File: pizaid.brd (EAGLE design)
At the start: 85 x 56 mm, 44 parts, among them X1 S4B-ZR, X2 DCJACK-R

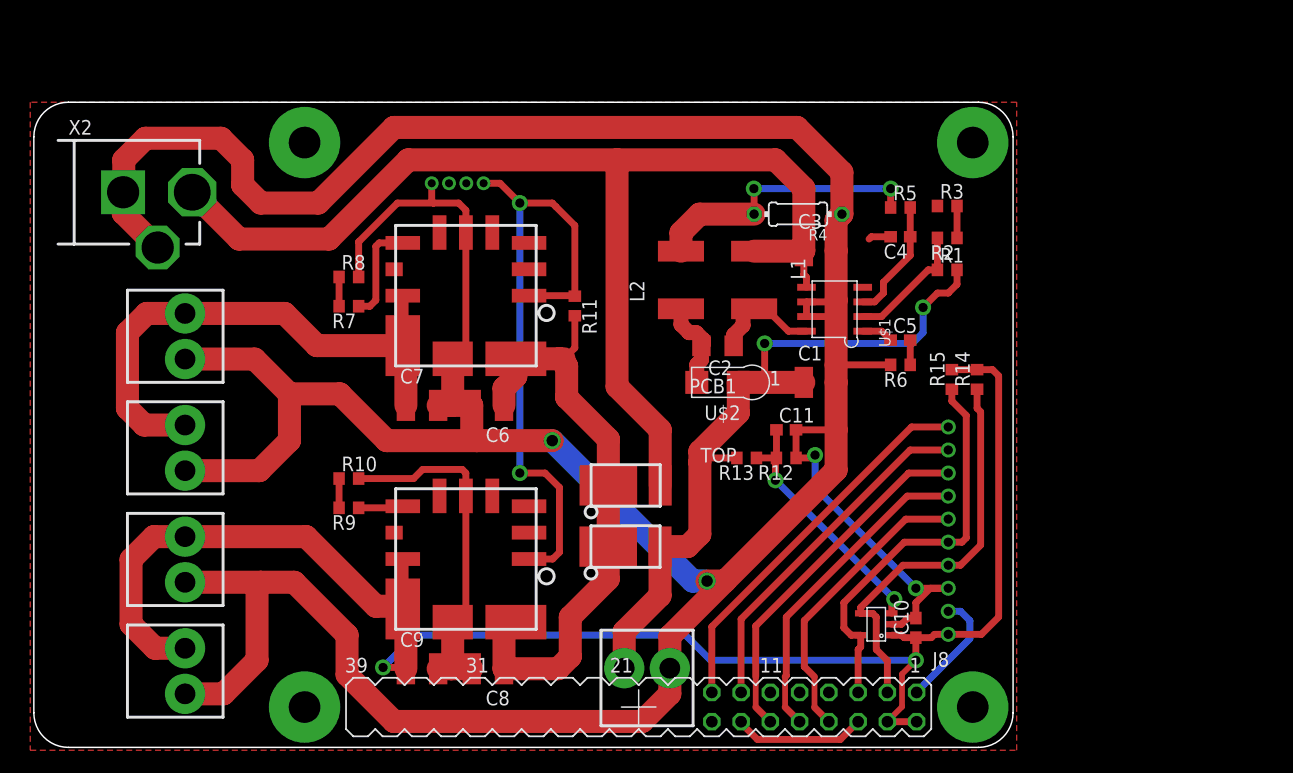
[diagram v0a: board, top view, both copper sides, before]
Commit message: modified board for stacking (ontheway)
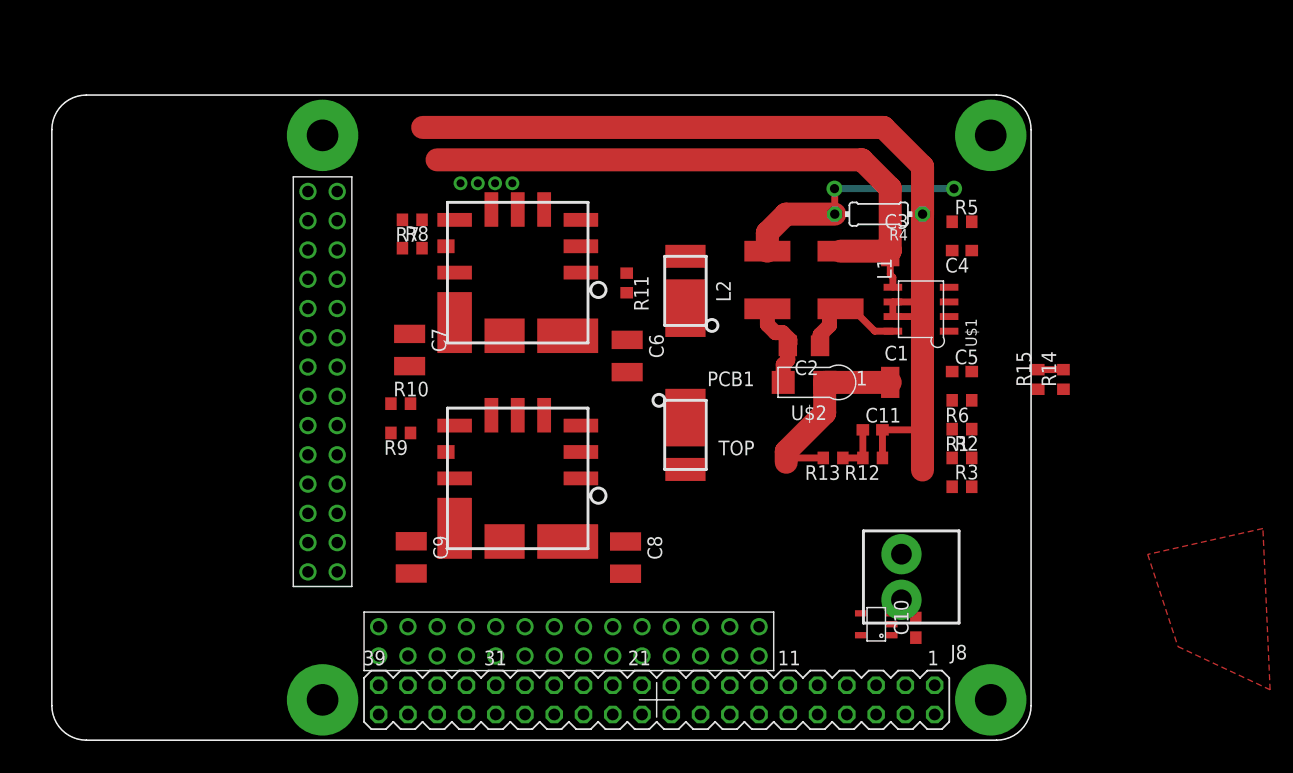
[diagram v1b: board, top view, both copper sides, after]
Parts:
- removed S1: 10B-PH, con-jst:S10B-PH
- removed U$14, U$15, U$9: B2P-VH, pizaid:B2P-VH
- removed X2: DCJACK-R, kamiki-dcjack:2DC-0005D100-R
- added U$3: CON_14X2, pizaid:CON_14X2
- PCB1: device pizaid:RASPBERRY_PI_B+ -> RASPBERRY_PI_Bplus:RASPBERRY_PI_B+
- U$8: value B2P-VH -> CON_14X2; device pizaid:B2P-VH -> pizaid:CON_14X2
- moved U$8 52.2 mm to (66.4, 13.8), turned to 180 degrees
- moved R3 24.4 mm to (84.0, 26.0)
- moved U$10 23.5 mm to (78.8, 18.2), turned to 90 degrees
- moved R2 19.1 mm to (84.0, 28.5), turned to 0 degrees
- moved U$5 17.7 mm to (60.0, 43.0), turned to 270 degrees
- moved C8 15.4 mm to (54.8, 19.8), turned to 270 degrees
- moved R1 13.9 mm to (84.0, 31.0), turned to 180 degrees
- moved C6 12.8 mm to (54.9, 37.3), turned to 270 degrees
- moved U$4 11.0 mm to (60.0, 30.5), turned to 90 degrees
- moved C9 9.71 mm to (36.2, 19.9), turned to 270 degrees
- moved R7 9.30 mm to (36.3, 49.2)
- moved U$7 8.32 mm to (45.4, 26.7)
- moved R10 7.91 mm to (35.3, 33.2)
- moved R9 7.91 mm to (35.3, 30.7)
- moved C1 7.50 mm to (79.2, 35.1)
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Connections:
- removed net 3V3@1: PCB1.1, S1.P$2
- removed net GND@1: PCB1.9
- removed net N$23: PCB1.13, S1.P$9
- new net B$1: PCB1.13, U$8.P$2
- new net B1: PCB1.15, U$8.P$4
- new net B10: PCB1.33, U$8.P$22
- new net B11: PCB1.35, U$8.P$24
- new net B12: PCB1.37, U$8.P$26
- new net B13: U$8.P$28
- new net B2: C10.1, PCB1.1, R14.2, R15.2, U$16.P$1, U$8.P$6
- new net B3: U$8.P$8
- new net B4: PCB1.21, U$8.P$10
- new net B5: PCB1.23, U$8.P$12
- new net B6: U$8.P$14
- new net B7: U$8.P$16
- new net B8: PCB1.29, U$8.P$18
- new net B9: PCB1.31, U$8.P$20
- new net GND@3: PCB1.25, PCB1.39, PCB1.9
- new net N$24: PCB1.26, U$8.P$13
- new net N$25: PCB1.24, U$8.P$11
- new net N$26: PCB1.22, U$8.P$9
- new net N$27: PCB1.18, U$8.P$5
- new net N$28: PCB1.16, U$8.P$3
- net 5V0@2: now also U$3.P$19, U$3.P$20, U$3.P$21, U$3.P$22, U$3.P$23; no longer C10.1, R14.2, R15.2, S1.P$1, U$14.P$1, U$16.P$1, U$9.P$1
- net GND: now also U$3.P$14, U$3.P$15, U$3.P$16, U$3.P$17, U$3.P$18, U$3.P$24, U$3.P$25, U$3.P$26, U$3.P$27, U$3.P$28, U$3.P$5, U$3.P$6, U$3.P$7, U$3.P$8; no longer S1.P$3, U$14.P$2, U$15.P$2, U$8.P$2, U$9.P$2, X2.2, X2.3
- net GND@4: now also PCB1.20, PCB1.30, PCB1.34, U$8.P$1, U$8.P$17, U$8.P$21, U$8.P$7
- net JNET: now also U$3.P$10, U$3.P$11, U$3.P$12, U$3.P$13, U$3.P$9; no longer U$15.P$1, U$8.P$1
- net N$13: now also PCB1.38, U$8.P$25; no longer PCB1.8, S1.P$6
- net N$16: no longer S1.P$5
- net N$20: no longer S1.P$4
- net N$21: now also PCB1.36, U$8.P$23; no longer PCB1.10, S1.P$7
- net N$22: now also PCB1.32, U$8.P$19; no longer PCB1.12, S1.P$8
- net N$9: now also PCB1.40, U$8.P$27; no longer PCB1.15, S1.P$10
- net VCC: now also U$3.P$1, U$3.P$2, U$3.P$3, U$3.P$4; no longer X2.1
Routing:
- net GND: track 380.9 -> 84.8 mm, vias 4 -> 0
- net 5V0@2: track 144.4 -> 0.71 mm, vias 2 -> 0
- net N$12: track 55.5 -> 0.00 mm, vias 2 -> 0
- net N$8: track 52.4 -> 0.00 mm
- net VCC: track 101.5 -> 53.4 mm
- net JNET: track 47.6 -> 0.38 mm
- net N$3: track 64.1 -> 17.4 mm, vias 2 -> 0
- net N$16: track 35.3 -> 0.00 mm
- net N$20: track 35.2 -> 0.00 mm
- net N$9: track 33.4 -> 0.00 mm
- net N$22: track 31.0 -> 0.00 mm
- net N$23: track 30.4 -> 0.00 mm
- net N$21: track 28.1 -> 0.00 mm
- net N$13: track 25.8 -> 0.00 mm
- net N$19: track 22.1 -> 4.18 mm, vias 2 -> 0
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
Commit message: added top board (ontheway)
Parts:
- moved R14 28.7 mm to (73.3, 14.3)
- moved R15 28.7 mm to (71.1, 14.3)
- moved U$10 2.92 mm to (77.2, 20.7)
- moved U$7 0.50 mm to (45.4, 27.2)
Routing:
- net B2: track 2.19 -> 0.00 mm
- net 5V0@2: track 0.71 -> 0.00 mm
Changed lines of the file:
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@@
 <plain>
 <rectangle x1="62.8125" y1="38.75" x2="77.8125" y2="48.75" layer="41"/>
-<rectangle x1="41.8125" y1="23.0625" x2="53.0625" y2="34.3125" layer="41"/>
+<rectangle x1="39.8125" y1="21.5625" x2="51.0625" y2="32.8125" layer="41"/>
 <wire x1="34.5" y1="45.4375" x2="3.125" y2="43.4375" width="0.1" layer="41"/>
 <wire x1="3.4375" y1="24.6875" x2="25.3125" y2="24.6875" width="0.1" layer="41"/>
@@
 <wire x1="34.5" y1="45.4375" x2="34.5" y2="48.875" width="0.1" layer="41"/>
 <rectangle x1="39.8125" y1="38.875" x2="51.0625" y2="50.125" layer="41"/>
-<rectangle x1="93.5625" y1="23" x2="104.8125" y2="34.25" layer="41"/>
 </plain>
 <attributes>
@@
 <element name="U$5" library="pizaid" package="POWERDI5" value="SBR15U50" x="60" y="43" rot="R270"/>
 <element name="U$6" library="pizaid" package="OKL-T/6" value="OKL-T/6" x="45.4425" y="44.585" rot="R180"/>
-<element name="U$7" library="pizaid" package="OKL-T/6" value="OKL-T/6" x="45.4425" y="26.725" rot="R180"/>
+<element name="U$7" library="pizaid" package="OKL-T/6" value="OKL-T/6" x="45.4425" y="27.225" rot="R180"/>
 <element name="C6" library="rcl" package="C3225" value="22u25V" x="54.94" y="37.3475" rot="R270"/>
 <element name="C7" library="rcl" package="C3225" value="22u16V" x="36.06" y="37.8675" rot="R270"/>
@@
 </element>
 <element name="R11" library="rcl" package="R0603" value="10k" x="54.8975" y="43.69" rot="R270"/>
-<element name="U$10" library="pizaid" package="B2P-VH" value="B2P-VH" x="78.75" y="18.165" rot="R90"/>
+<element name="U$10" library="pizaid" package="B2P-VH" value="B2P-VH" x="77.25" y="20.665" rot="R90"/>
 <element name="U$16" library="pizaid" package="SOT-23" value="MCP3021" x="76.5625" y="14.0625" rot="R90"/>
 <element name="C10" library="rcl" package="C0603" value="0.1u" x="80" y="13.75" rot="R90"/>
@@
 <element name="R12" library="rcl" package="R0603" value="10k" x="76.25" y="28.5" rot="R180"/>
 <element name="R13" library="rcl" package="R0603" value="10k" x="72.8125" y="28.5" rot="R180"/>
-<element name="R14" library="rcl" package="R0603" value="2.2k" x="92.8125" y="35.3125" rot="R90"/>
-<element name="R15" library="rcl" package="R0603" value="2.2k" x="90.625" y="35.3125" rot="R90"/>
+<element name="R14" library="rcl" package="R0603" value="2.2k" x="73.3125" y="14.3125" rot="R90"/>
+<element name="R15" library="rcl" package="R0603" value="2.2k" x="71.125" y="14.3125" rot="R90"/>
 <element name="PCB1" library="RASPBERRY_PI_Bplus" package="RASPBERRY_PI_B+" value="RASPBERRY_PI_B+" x="90" y="60" rot="R180"/>
 <element name="U$3" library="pizaid" package="CON_14X2" value="CON_14X2" x="27.23" y="51.63" rot="R270"/>
@@
 <wire x1="45.4425" y1="50.065" x2="40.475" y2="52.3425" width="0" layer="19" extent="1-1"/>
 <wire x1="37.1325" y1="46.7075" x2="40.475" y2="52.3425" width="0" layer="19" extent="1-1"/>
-<wire x1="78.75" y1="20.145" x2="83.15" y2="26" width="0" layer="19" extent="1-1"/>
-<wire x1="80" y1="14.6" x2="78.75" y2="20.145" width="0" layer="19" extent="1-1"/>
+<wire x1="77.25" y1="22.645" x2="83.15" y2="26" width="0" layer="19" extent="1-1"/>
+<wire x1="80" y1="14.6" x2="77.25" y2="22.645" width="0" layer="19" extent="1-1"/>
 <wire x1="77.9125" y1="14.0625" x2="80" y2="14.6" width="0" layer="19" extent="1-1"/>
 <wire x1="29.77" y1="46.55" x2="37.1325" y2="46.7075" width="0" layer="19" extent="1-1"/>
@@
 <wire x1="27.23" y1="18.61" x2="29.77" y2="18.61" width="0" layer="19" extent="1-1"/>
 <wire x1="36.2" y1="18.4675" x2="29.77" y2="18.61" width="0" layer="19" extent="1-1"/>
-<wire x1="44.2975" y1="21.245" x2="36.2" y2="18.4675" width="0" layer="19" extent="1-1"/>
+<wire x1="44.2975" y1="21.745" x2="36.2" y2="18.4675" width="0" layer="19" extent="1-1"/>
 <wire x1="44.2975" y1="39.105" x2="36.06" y2="36.4675" width="0" layer="19" extent="1-1"/>
-<wire x1="45.4425" y1="32.205" x2="45.4375" y2="39.1875" width="0" layer="19" extent="1-1"/>
+<wire x1="45.4425" y1="32.705" x2="45.4375" y2="39.1875" width="0" layer="19" extent="1-1"/>
 <wire x1="28.5" y1="56.5" x2="37.1875" y2="57.1875" width="0" layer="19" extent="1-1"/>
 <wire x1="86.5" y1="7.5" x2="80" y2="14.6" width="0" layer="19" extent="1-1"/>
 <wire x1="54.94" y1="35.9475" x2="45.4375" y2="39.1875" width="0" layer="19" extent="1-1"/>
-<wire x1="54.8" y1="18.4475" x2="44.2975" y2="21.245" width="0" layer="19" extent="1-1"/>
+<wire x1="54.8" y1="18.4475" x2="44.2975" y2="21.745" width="0" layer="19" extent="1-1"/>
 <wire x1="28.5" y1="7.5" x2="29.77" y2="18.61" width="0" layer="19" extent="1-1"/>
 </signal>
@@
 <wire x1="77.775" y1="35.0575" x2="83.15" y2="31" width="0" layer="19" extent="1-1"/>
 <wire x1="60" y1="27.5" x2="68.75" y2="28.125" width="0" layer="19" extent="1-1"/>
-<wire x1="78.75" y1="16.185" x2="71.9625" y2="28.5" width="0" layer="19" extent="1-1"/>
+<wire x1="77.25" y1="18.685" x2="71.9625" y2="28.5" width="0" layer="19" extent="1-1"/>
 <wire x1="77.775" y1="35.0575" x2="72.085" y2="35.0575" width="2" layer="1"/>
 </signal>
@@
 <wire x1="54.8" y1="21.2475" x2="60.795" y2="26.1" width="0" layer="19" extent="1-1"/>
 <wire x1="60" y1="32" x2="54.8" y2="21.2475" width="0" layer="19" extent="1-1"/>
-<wire x1="49.7775" y1="21.245" x2="54.8" y2="21.2475" width="0" layer="19" extent="1-1"/>
+<wire x1="49.7775" y1="21.745" x2="54.8" y2="21.2475" width="0" layer="19" extent="1-1"/>
 </signal>
 <signal name="N$14">
 <contactref element="U$7" pad="P$6"/>
 <contactref element="R9" pad="1"/>
-<wire x1="39.8275" y1="31.17" x2="39.9625" y2="31.305" width="0.6" layer="1"/>
-<wire x1="36.1325" y1="30.67" x2="39.8275" y2="31.17" width="0" layer="19" extent="1-1"/>
+<wire x1="36.1325" y1="30.67" x2="39.9625" y2="31.805" width="0" layer="19" extent="1-1"/>
 </signal>
 <signal name="N$15">
@@
 <wire x1="50.9225" y1="44.585" x2="54.8975" y2="44.54" width="0" layer="19" extent="1-1"/>
 <wire x1="44.975" y1="52.3425" x2="50.9225" y2="44.585" width="0" layer="19" extent="1-1"/>
-<wire x1="50.9225" y1="26.725" x2="50.9225" y2="44.585" width="0" layer="19" extent="1-1"/>
+<wire x1="50.9225" y1="27.225" x2="50.9225" y2="44.585" width="0" layer="19" extent="1-1"/>
 </signal>
 <signal name="N$16">
@@
 <contactref element="R15" pad="1"/>
 <contactref element="PCB1" pad="5"/>
-<wire x1="75.2125" y1="13.1125" x2="90.625" y2="34.4625" width="0" layer="19" extent="1-1"/>
+<wire x1="75.2125" y1="13.1125" x2="71.125" y2="13.4625" width="0" layer="19" extent="1-1"/>
 <wire x1="76.55" y1="8.77" x2="75.2125" y2="13.1125" width="0" layer="19" extent="1-1"/>
 </signal>
@@
 <contactref element="R14" pad="1"/>
 <contactref element="PCB1" pad="3"/>
-<wire x1="75.2125" y1="15.0125" x2="92.8125" y2="34.4625" width="0" layer="19" extent="1-1"/>
+<wire x1="75.2125" y1="15.0125" x2="73.3125" y2="13.4625" width="0" layer="19" extent="1-1"/>
 <wire x1="79.09" y1="8.77" x2="75.2125" y2="15.0125" width="0" layer="19" extent="1-1"/>
 </signal>
@@
 <contactref element="PCB1" pad="2"/>
 <contactref element="PCB1" pad="4"/>
-<wire x1="39.7275" y1="22.625" x2="39.9625" y2="22.39" width="2" layer="1"/>
-<wire x1="40.2325" y1="22.12" x2="39.9625" y2="22.39" width="2" layer="1"/>
 <contactref element="U$3" pad="P$19"/>
 <contactref element="U$3" pad="P$21"/>
@@
 <contactref element="U$3" pad="P$22"/>
 <wire x1="79.09" y1="6.23" x2="81.63" y2="6.23" width="0" layer="19" extent="1-1"/>
-<wire x1="40.2325" y1="22.12" x2="79.09" y2="6.23" width="0" layer="19" extent="1-1"/>
-<wire x1="36.2" y1="21.2675" x2="39.7275" y2="22.625" width="0" layer="19" extent="1-1"/>
-<wire x1="39.9625" y1="26.725" x2="39.7275" y2="22.625" width="0" layer="19" extent="1-1"/>
+<wire x1="39.9625" y1="22.89" x2="79.09" y2="6.23" width="0" layer="19" extent="1-1"/>
+<wire x1="39.9625" y1="27.225" x2="39.9625" y2="22.89" width="0" layer="19" extent="1-1"/>
+<wire x1="36.2" y1="21.2675" x2="39.9625" y2="22.89" width="0" layer="19" extent="1-1"/>
 <wire x1="29.77" y1="26.23" x2="36.2" y2="21.2675" width="0" layer="19" extent="1-1"/>
 <wire x1="29.77" y1="28.77" x2="29.77" y2="26.23" width="0" layer="19" extent="1-1"/>
@@
 <contactref element="R15" pad="2"/>
 <contactref element="R14" pad="2"/>
-<wire x1="90.625" y1="36.1625" x2="92.8125" y2="36.1625" width="0.6" layer="1"/>
-<wire x1="80" y1="12.9" x2="90.625" y2="36.1625" width="0" layer="19" extent="1-1"/>
+<wire x1="71.125" y1="15.1625" x2="73.3125" y2="15.1625" width="0" layer="19" extent="1-16"/>
+<wire x1="80" y1="12.9" x2="71.125" y2="15.1625" width="0" layer="19" extent="1-1"/>
 <wire x1="77.9125" y1="13.1125" x2="80" y2="12.9" width="0" layer="19" extent="1-1"/>
 <wire x1="81.63" y1="8.77" x2="80" y2="12.9" width="0" layer="19" extent="1-1"/>

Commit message: continuing placement.....................
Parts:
- moved U$5 11.8 mm to (62.5, 31.5), turned to 180 degrees
- moved C11 9.51 mm to (76.8, 21.4)
- moved R12 9.51 mm to (76.8, 19.0)
- moved R13 9.51 mm to (73.3, 19.0)
- moved R1 8.00 mm to (84.0, 23.0)
- moved R2 8.00 mm to (84.0, 20.5)
- moved U$10 7.52 mm to (76.8, 28.2)
- moved R3 7.50 mm to (84.0, 18.5)
- moved U$4 4.30 mm to (62.5, 27.0), turned to 180 degrees
- moved R8 2.91 mm to (36.3, 43.8), turned to 270 degrees
- moved R7 1.87 mm to (36.3, 47.3), turned to 270 degrees
- moved C5 1.00 mm to (84.0, 37.0)
- moved R6 1.00 mm to (84.0, 34.5)
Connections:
- net GND: now also U$3.P$1, U$3.P$2, U$3.P$3, U$3.P$4; no longer U$3.P$5, U$3.P$6, U$3.P$7, U$3.P$8
- net VCC: now also U$3.P$5, U$3.P$6, U$3.P$7, U$3.P$8; no longer U$3.P$1, U$3.P$2, U$3.P$3, U$3.P$4
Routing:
- net GND: track 84.8 -> 173.9 mm
- net VCC: track 53.4 -> 98.6 mm
- net N$8: track 0.00 -> 37.4 mm
- net 5V0@2: track 0.00 -> 25.7 mm
- net JNET: track 0.38 -> 21.8 mm
- net N$3: track 17.4 -> 25.4 mm
- net N$19: track 4.18 -> 0.00 mm

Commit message: updated second layer
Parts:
- removed X1: S4B-ZR, con-jst:S4B-ZR
- added R16: 10k, rcl:R0603
- moved R10 5.07 mm to (36.0, 28.2), turned to 270 degrees
- moved R3 4.03 mm to (80.0, 18.0)
- moved R1 2.50 mm to (84.0, 20.5)
- moved R2 2.50 mm to (84.0, 18.0)
- moved R14 1.77 mm to (72.0, 15.5), turned to 180 degrees
- moved R13 1.65 mm to (72.0, 18.0)
- moved R15 1.58 mm to (72.0, 13.0), turned to 180 degrees
- moved R9 1.40 mm to (36.0, 31.9), turned to 270 degrees
- moved R12 1.25 mm to (76.0, 18.0)
- moved C11 1.20 mm to (76.0, 20.5)
- moved C10 0.70 mm to (80.3, 13.1)
- moved R11 0.33 mm to (55.0, 44.0)
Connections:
- new net GIRD: C6.1, C8.1, R11.2, R16.2, U$4.P$1, U$5.P$1, U$6.P$2, U$7.P$2
- net GND: no longer X1.1
- net N$12: now also R16.1; no longer R11.1, U$6.P$1, X1.4
- net N$8: now also R11.1, U$6.P$1; no longer C6.1, C8.1, R11.2, U$4.P$1, U$5.P$1, U$6.P$2, U$7.P$2
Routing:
- net 5V0@2: track 25.7 -> 91.2 mm, vias 0 -> 1
- net GND@4: track 0.00 -> 64.0 mm
- net GND: track 173.9 -> 232.0 mm, vias 0 -> 3
- net GIRD: track 0.00 -> 46.8 mm
- net GND@3: track 0.00 -> 40.2 mm
- net B2: track 0.00 -> 33.6 mm, vias 0 -> 2
- net N$8: track 37.4 -> 4.19 mm
- net N$10: track 0.00 -> 26.3 mm
- net N$3: track 25.4 -> 46.2 mm
- net N$20: track 0.00 -> 11.4 mm
- net N$19: track 0.00 -> 9.85 mm
- net N$9: track 0.00 -> 8.68 mm
- net N$28: track 0.00 -> 8.68 mm
- net N$24: track 0.00 -> 8.68 mm
- net N$21: track 0.00 -> 8.68 mm
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- added copper zone on layer 16, net GND

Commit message: completed rev1
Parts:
- removed U$16: MCP3021, pizaid:SOT-23
- added U$9: MCP3425, pizaid:SOT-23-6
- moved R14 9.66 mm to (81.0, 12.0), turned to 0 degrees
- moved C10 1.50 mm to (80.3, 14.6)
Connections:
- removed net GND@3: PCB1.25, PCB1.39, PCB1.9
- removed net GND@4: PCB1.14, PCB1.20, PCB1.30, PCB1.34, PCB1.6, U$8.P$1, U$8.P$17, U$8.P$21, U$8.P$7
- net B2: now also U$9.P$5; no longer U$16.P$1
- net GND: now also PCB1.14, PCB1.20, PCB1.25, PCB1.30, PCB1.34, PCB1.39, PCB1.6, PCB1.9, U$8.P$1, U$8.P$17, U$8.P$21, U$8.P$7, U$9.P$2, U$9.P$6; no longer U$16.P$2
- net N$16: now also U$9.P$3; no longer U$16.P$5
- net N$19: now also U$9.P$1; no longer U$16.P$3
- net N$20: now also U$9.P$4; no longer U$16.P$4
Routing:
- net GND: track 232.0 -> 337.2 mm, vias 3 -> 84
- net GND@4: track 64.0 -> 0.00 mm
- net GND@3: track 40.2 -> 0.00 mm
- net N$20: track 11.4 -> 7.70 mm
- net N$19: track 9.85 -> 7.10 mm
- net N$16: track 7.32 -> 8.24 mm
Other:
- board size 85 x 56 mm -> 65 x 56 mm
- board text added: "Pizaid battery manager"
- board text added: "rev. 1 2014/10/01"
